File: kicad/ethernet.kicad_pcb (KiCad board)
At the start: 2 copper layers, 67 x 57 mm, 41 parts, among them J1 RJ45_Abracon_ARJP11A-MASA-B-A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, J2 Conn_Coaxial, J3 MSP-FET, SW1 KSC701, SW2 KSC701, U1 MSP432E401Y, U2 MAX-8Q, X1 TXEAADSANF-25.000000

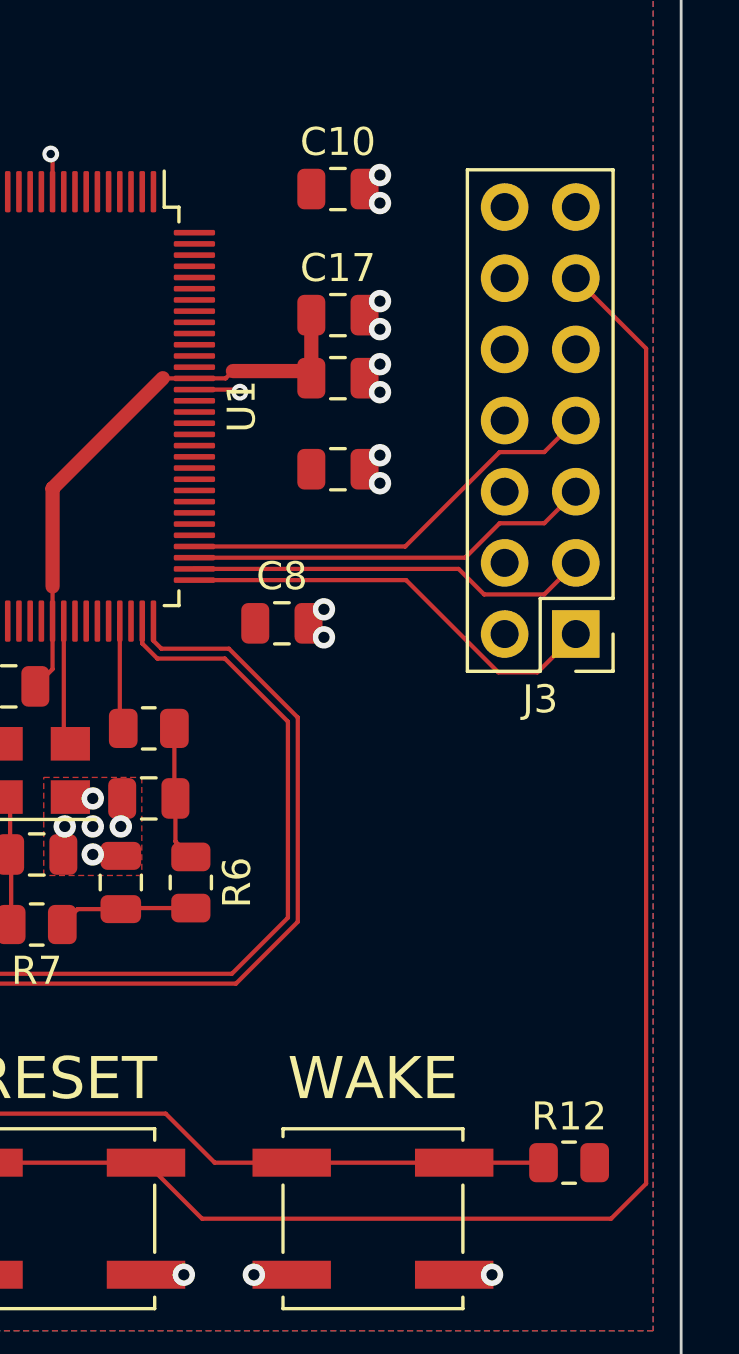
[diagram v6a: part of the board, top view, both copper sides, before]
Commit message: begin PTP implementation
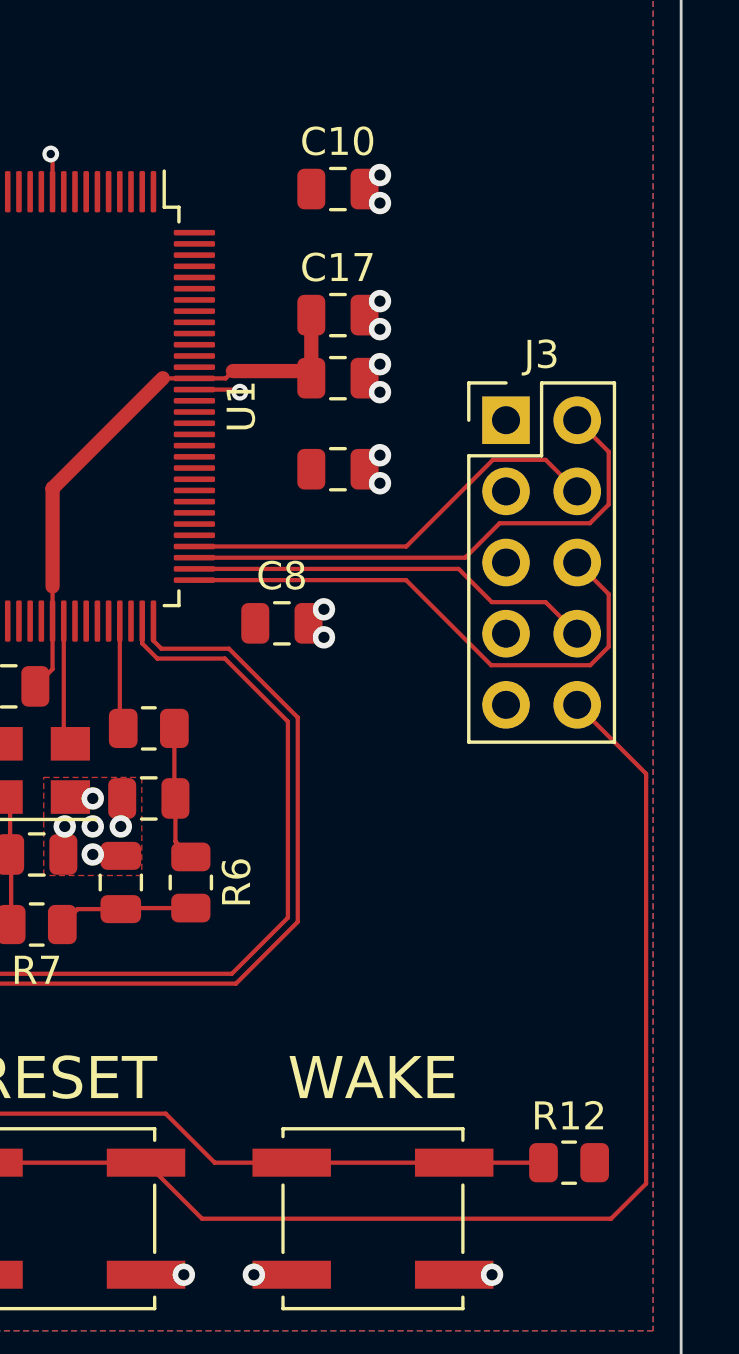
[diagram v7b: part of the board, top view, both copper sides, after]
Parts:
- J3: value MSP-FET -> JTAG; footprint Connector_PinHeader_2.54mm:PinHeader_2x07_P2.54mm_Vertical -> Connector_PinHeader_2.54mm:PinHeader_2x05_P2.54mm_Vertical
- moved J3 8.03 mm to (83.8, 36.5), turned to 0 degrees
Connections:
- J3 pad 1: Net-(J3-Pad1) -> +3V3
- J3 pad 10: unconnected-(J3-Pad10) -> ~{RST}
- J3 pad 2: unconnected-(J3-Pad2) -> Net-(U1-Pad99)
- J3 pad 3: Net-(J3-Pad3) -> GND
- J3 pad 4: +3V3 -> Net-(U1-Pad100)
- J3 pad 5: Net-(J3-Pad5) -> GND
- J3 pad 6: unconnected-(J3-Pad6) -> Net-(U1-Pad97)
- J3 pad 7: Net-(J3-Pad7) -> unconnected-(J3-Pad7)
- J3 pad 8: unconnected-(J3-Pad8) -> Net-(U1-Pad98)
- U1 pad 100: Net-(J3-Pad7) -> Net-(U1-Pad100)
- U1 pad 97: Net-(J3-Pad1) -> Net-(U1-Pad97)
- U1 pad 98: Net-(J3-Pad3) -> Net-(U1-Pad98)
- U1 pad 99: Net-(J3-Pad5) -> Net-(U1-Pad99)
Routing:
- net Net-(U1-Pad97): track 0.00 -> 19.8 mm
- net Net-(U1-Pad99): track 0.00 -> 19.0 mm
- net Net-(J3-Pad1): track 15.5 -> 0.00 mm
- net Net-(J3-Pad7): track 15.5 -> 0.00 mm
- net Net-(U1-Pad100): track 0.00 -> 15.4 mm
- net ~{RST}: track 82.0 -> 66.7 mm
- net Net-(U1-Pad98): track 0.00 -> 14.6 mm
- net Net-(J3-Pad5): track 14.6 -> 0.00 mm
- net Net-(J3-Pad3): track 14.5 -> 0.00 mm

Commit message: updating schematic
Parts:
- removed C3: 100n, Capacitor_SMD:C_0805_2012Metric
- removed R6, R7: 10k, Resistor_SMD:R_0805_2012Metric
- removed X1: TXEAADSANF-25.000000, Oscillator:Oscillator_SMD_SeikoEpson_SG8002CE-4Pin_3.2x2.5mm
- added BT1: NiMH, Battery:BatteryHolder_Keystone_2466_1xAAA, F.Cu at (185.0, 85.0)
- added BT2: NiMH, Battery:BatteryHolder_Keystone_2466_1xAAA, F.Cu at (185.0, 54.9)
- added BT3: NiMH, Battery:BatteryHolder_Keystone_2466_1xAAA, F.Cu at (185.0, 70.0)
- added BT4: NiMH, Battery:BatteryHolder_Keystone_2466_1xAAA, F.Cu at (237.1, 54.9)
- added R15: 110k, Resistor_SMD:R_0805_2012Metric, F.Cu at (187.9, 97.0)
- added R16: 110k, Resistor_SMD:R_0805_2012Metric, F.Cu at (192.3, 94.0)
- added R17: 110k, Resistor_SMD:R_0805_2012Metric, F.Cu at (196.7, 94.0)
- added R18: 110k, Resistor_SMD:R_0805_2012Metric, F.Cu at (183.5, 97.0)
- added R19: 330k, Resistor_SMD:R_0805_2012Metric, F.Cu at (235.5, 63.9)
- added R20: 330k, Resistor_SMD:R_0805_2012Metric, F.Cu at (183.5, 94.0)
- added R21: 330k, Resistor_SMD:R_0805_2012Metric, F.Cu at (187.9, 94.0)
- added R22: 330k, Resistor_SMD:R_0805_2012Metric, F.Cu at (201.1, 94.0)
- added Y1: NX3225GA-25.000M-STD-CRG-2, Crystal:Crystal_SMD_3225-4Pin_3.2x2.5mm, F.Cu at (150.4, 63.8)
- C1, C2: value 100n -> 12p
- R5: value 10k -> 2k
- moved C2 85.8 mm to (155.2, 63.0), turned to 0 degrees
- moved R5 85.8 mm to (154.4, 67.5)
- moved C1 80.9 mm to (150.0, 67.5), turned to 0 degrees
- moved J1 80.1 mm to (99.7, 87.0)
- moved TR1 80.1 mm to (112.1, 68.2)
- moved U2 80.1 mm to (116.7, 105.5)
- moved C10 80.1 mm to (138.5, 80.5)
- moved C11 80.1 mm to (113.5, 84.5)
- moved C12 80.1 mm to (103.2, 77.7)
- moved C13 80.1 mm to (92.5, 80.0)
- moved C14 80.1 mm to (114.5, 115.8)
- moved C15 80.1 mm to (126.8, 98.2)
- moved C16 80.1 mm to (138.5, 87.2)
- moved C17 80.1 mm to (138.5, 85.0)
- moved C4 80.1 mm to (124.2, 101.2)
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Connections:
- net uPPS renamed ePPS
- C1 pad 1: Net-(C1-Pad1) -> Net-(U1-Pad88)
- C2 pad 1: Net-(C2-Pad1) -> GND
- C2 pad 2: GND -> Net-(C2-Pad2)
- R5 pad 1: Net-(R5-Pad1) -> Net-(U1-Pad89)
- R5 pad 2: Net-(C1-Pad1) -> Net-(C2-Pad2)
- U1 pad 12: unconnected-(U1-Pad12) -> Net-(U1-Pad12)
- U1 pad 13: unconnected-(U1-Pad13) -> Net-(U1-Pad13)
- U1 pad 14: unconnected-(U1-Pad14) -> Net-(U1-Pad14)
- U1 pad 15: unconnected-(U1-Pad15) -> Net-(U1-Pad15)
- U1 pad 89: unconnected-(U1-Pad89) -> Net-(U1-Pad89)
- U1 pad 93: Net-(R5-Pad1) -> +3V3
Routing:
- net Net-(C2-Pad1): track 4.83 -> 0.00 mm
- net Net-(C1-Pad1): track 4.83 -> 0.00 mm
- net Net-(C3-Pad1): track 4.67 -> 0.00 mm
- net Net-(U1-Pad88): track 4.48 -> 0.00 mm
- net Net-(R5-Pad1): track 3.88 -> 0.00 mm
- net GND: vias 49 -> 44
- removed copper zone on F.Cu, net GND
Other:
- board size 67 x 57 mm -> 120 x 90 mm
